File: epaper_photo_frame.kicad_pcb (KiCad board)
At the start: 2 copper layers, 98 parts, among them IC1 ST1PS03AQTR, IC2 CM1624-08DE, J1 47352-1001, J2 Conn_ARM_JTAG_SWD_20, J3 Battery Connector, J4 54104-5031, Q1 BSS138, Q2 SI2301CDS-T1-E3, Q3 AO3401A, Q31 AO3401A, Q32 S8050, U1 SIP32402ADNP-T1GE4, U2 RT9193-33GB, U3 STM32L431CBT6, Y1 NX3215SA-32.768K-STD-MUA-14

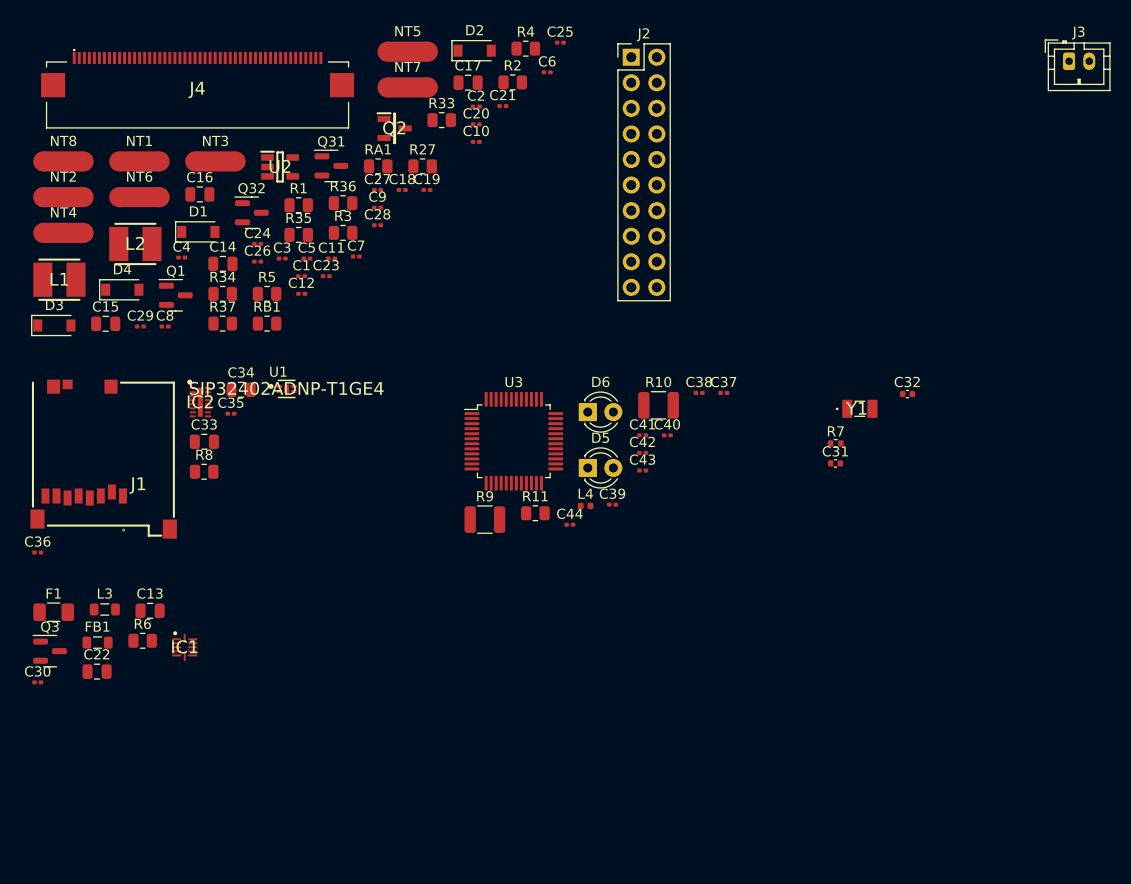
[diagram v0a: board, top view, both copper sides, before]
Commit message: Added preliminary PCL layout
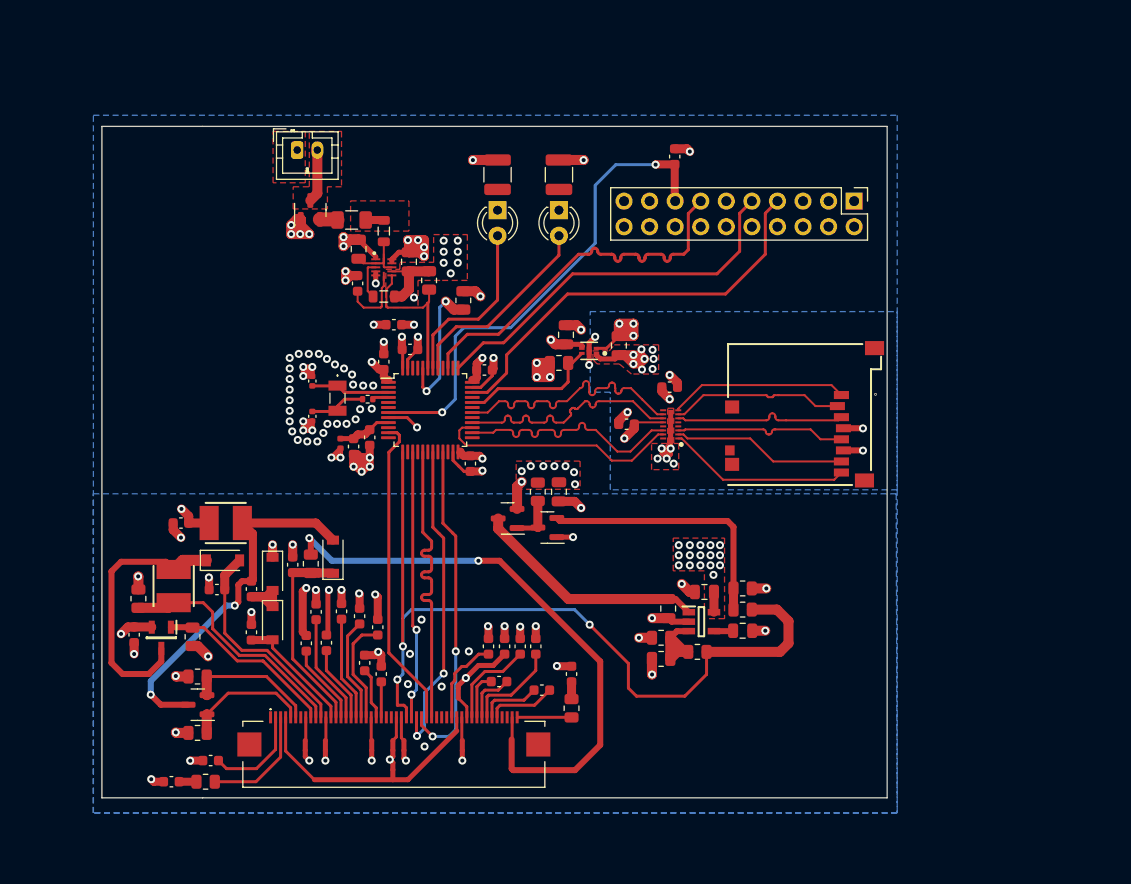
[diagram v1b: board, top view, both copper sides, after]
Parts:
- C1, C10, C11, C12, C18, C19, C2, C20, C21, C23, C24, C25, C26, C27, C28, C29, C3, C30, C35, C36, C37, C38, C39, C4, C40, C41, C42, C43, C44, C5, C6, C7, C8, C9: footprint Capacitor_SMD:C_0201_0603Metric -> Capacitor_SMD:C_0603_1608Metric
- NT1, NT2, NT3, NT4, NT5, NT6, NT7, NT8: footprint NetTie:NetTie-2_SMD_Pad2.0mm -> NetTie:NetTie-2_SMD_Pad0.5mm
- moved J3 77.2 mm to (126.4, 77.2)
- moved C2 73.6 mm to (113.9, 139.9), turned to 180 degrees
- moved J1 72.8 mm to (184.4, 96.4), turned to 90 degrees
- moved J4 68.3 mm to (136.0, 133.9)
- moved R4 67.1 mm to (116.0, 125.5), turned to 90 degrees
- moved R2 66.8 mm to (116.5, 129.4), turned to 180 degrees
- moved NT7 65.9 mm to (129.2, 136.3), turned to -90 degrees
- moved NT2 64.1 mm to (137.0, 136.3), turned to -90 degrees
- moved NT5 63.9 mm to (142.4, 131.1), turned to 90 degrees
- moved C16 63.8 mm to (166.8, 121.0)
- moved C25 63.8 mm to (146.4, 129.9), turned to 180 degrees
- moved RA1 63.5 mm to (117.3, 139.9), turned to 180 degrees
- moved NT3 63.0 mm to (142.8, 136.3), turned to -90 degrees
- moved NT8 62.8 mm to (127.2, 136.3), turned to -90 degrees
- moved NT6 62.7 mm to (135.9, 139.2), turned to 90 degrees
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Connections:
- IC2 pad 1: unconnected-(IC2-Pad1) -> /Micro SD/SD_DATA1
- IC2 pad 10: /Micro SD/SD_DATA3 -> /MCU/SDC_SPI_NSS
- IC2 pad 11: /Micro SD/SD_CMD -> /MCU/SDC_SPI_MOSI
- IC2 pad 14: /Micro SD/SD_CLK -> /MCU/SDC_SPI_SCK
- IC2 pad 15: /Micro SD/SD_DATA0 -> /MCU/SDC_SPI_MISO
- IC2 pad 16: /Micro SD/SD_DATA1 -> unconnected-(IC2-Pad16)
- IC2 pad 2: /MCU/SDC_SPI_MISO -> /Micro SD/SD_DATA0
- IC2 pad 3: /MCU/SDC_SPI_SCK -> /Micro SD/SD_CLK
- IC2 pad 6: /MCU/SDC_SPI_MOSI -> /Micro SD/SD_CMD
- IC2 pad 7: /MCU/SDC_SPI_NSS -> /Micro SD/SD_DATA3
- IC2 pad 8: unconnected-(IC2-Pad8) -> /Micro SD/SD_DATA2
- IC2 pad 9: /Micro SD/SD_DATA2 -> unconnected-(IC2-Pad9)
- J4 pad 34: /Display Adapter/EPD_D1 -> unconnected-(J4-Pad34)
- J4 pad 35: /Display Adapter/EPD_D2 -> unconnected-(J4-Pad35)
- J4 pad 36: /Display Adapter/EPD_D3 -> unconnected-(J4-Pad36)
- U3 pad 13: /Display Adapter/EPD_CS -> /Display Adapter/EPD_RST
- U3 pad 15: /Display Adapter/EPD_DC -> /Display Adapter/EPD_BUSY
- U3 pad 19: /Display Adapter/EPD_RST -> /Display Adapter/EPD_DC
- U3 pad 21: /Display Adapter/EPD_BUSY -> /Display Adapter/EPD_CS
- U3 pad 41: unconnected-(U3-Pad41) -> /MCU/LED_ERR_IN
- U3 pad 42: unconnected-(U3-Pad42) -> /MCU/LED_BUSY_IN
- U3 pad 45: /MCU/LED_ERR_IN -> unconnected-(U3-Pad45)
- U3 pad 46: /MCU/LED_BUSY_IN -> unconnected-(U3-Pad46)
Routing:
- net GND: track 0.00 -> 181.5 mm, vias 0 -> 120
- net /Display Adapter/EPD_RST: track 0.00 -> 83.6 mm, vias 0 -> 3
- net /Display Adapter/VGH: track 0.00 -> 59.0 mm, vias 0 -> 2
- net /Debug Connector/NRST: track 0.00 -> 49.3 mm, vias 0 -> 2
- net /Debug Connector/SWDIO: track 0.00 -> 41.6 mm
- net /Debug Connector/SWDCLK: track 0.00 -> 38.3 mm
- net /Debug Connector/SWO: track 0.00 -> 38.1 mm
- net /Display Adapter/3v3_HPF: track 0.00 -> 36.6 mm, vias 0 -> 2
- net /Display Adapter/EPD_CS: track 0.00 -> 33.0 mm, vias 0 -> 2
- net /Display Adapter/EPD_DC: track 0.00 -> 31.7 mm, vias 0 -> 2
- net /Display Adapter/EPD_SCK: track 0.00 -> 31.2 mm
- net /Display Adapter/EPD_DIN: track 0.00 -> 31.0 mm
- net /Debug Connector/MCU_VDD: track 0.00 -> 29.2 mm, vias 0 -> 24
- net /MCU/SDC_SPI_NSS: track 0.00 -> 26.9 mm
- net /Display Adapter/VPC_1: track 0.00 -> 26.8 mm
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- added copper zone on B.Cu, net /Debug Connector/MCU_VDD
- added copper zone on F.Cu, net /Debug Connector/MCU_VDD
- added copper zone on B.Cu, net /Display Adapter/3v3
- added copper zone on F.Cu, net /Display Adapter/3v3
- added copper zone on B.Cu, net /Micro SD/3v3
- added copper zone on F.Cu, net /Micro SD/3v3
- added copper zone on F.Cu, net /Power Supply/VBAT_IN
- added copper zone on F.Cu, net /Power Supply/VBAT_IN_FUSE_CHECKED
- added copper zone on F.Cu, net GND
- added copper zone on In1.Cu, net GND
- added copper zone on In2.Cu, net GND
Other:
- board outline added: 78 x 66.7 mm
- copper layers 2 -> 4
- rule pad_to_mask_clearance: 0 -> 0.06

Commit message: Revision 1 of the board that was manufactured
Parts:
- added H1: MountingHole, MountingHole:MountingHole_3.2mm_M3, F.Cu at (105.8, 75.7)
- added H2: MountingHole, MountingHole:MountingHole_3.2mm_M3, F.Cu at (181.2, 75.7)
- added H3: MountingHole, MountingHole:MountingHole_3.2mm_M3, F.Cu at (105.8, 137.7)
- added H4: MountingHole, MountingHole:MountingHole_3.2mm_M3, F.Cu at (181.2, 137.7)
- added R12: 5k, Resistor_SMD:R_1206_3216Metric, F.Cu at (142.0, 78.2)
- Q32: footprint Package_TO_SOT_SMD:SOT-23 -> Package_TO_SOT_SMD:SOT-23-3
- R10: value 42R2 -> 47k
- R9: value 78R7 -> 47k
- moved C38 0.50 mm to (136.0, 94.0)
- moved Q32 0.11 mm to (151.4, 114.7)
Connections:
- R10 pad 2: GND -> /MCU/LED_BUSY_OUT_2
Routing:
- net /Display Adapter/GNDA+(GND): track 4.64 -> 9.61 mm
- net /Debug Connector/SWDCLK: track 38.3 -> 41.4 mm
- net /Debug Connector/SWO: track 38.1 -> 35.1 mm
- net /MCU/LED_BUSY_OUT_2: track 0.00 -> 2.91 mm
- net /MCU/SDC_SPI_NSS: track 26.9 -> 24.3 mm
- net /MCU/LED_ERR_OUT: track 0.00 -> 2.06 mm
- net /MCU/LED_BUSY_OUT: track 0.00 -> 2.06 mm
- net (no net): track 0.75 -> 0.00 mm
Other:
- board size 78 x 66.7 mm -> 83.1 x 69.5 mm
- rule pad_to_mask_clearance: 0.06 -> 0.05
- board text added: "+"
- board text added: "JLCJLCJLCJLC"

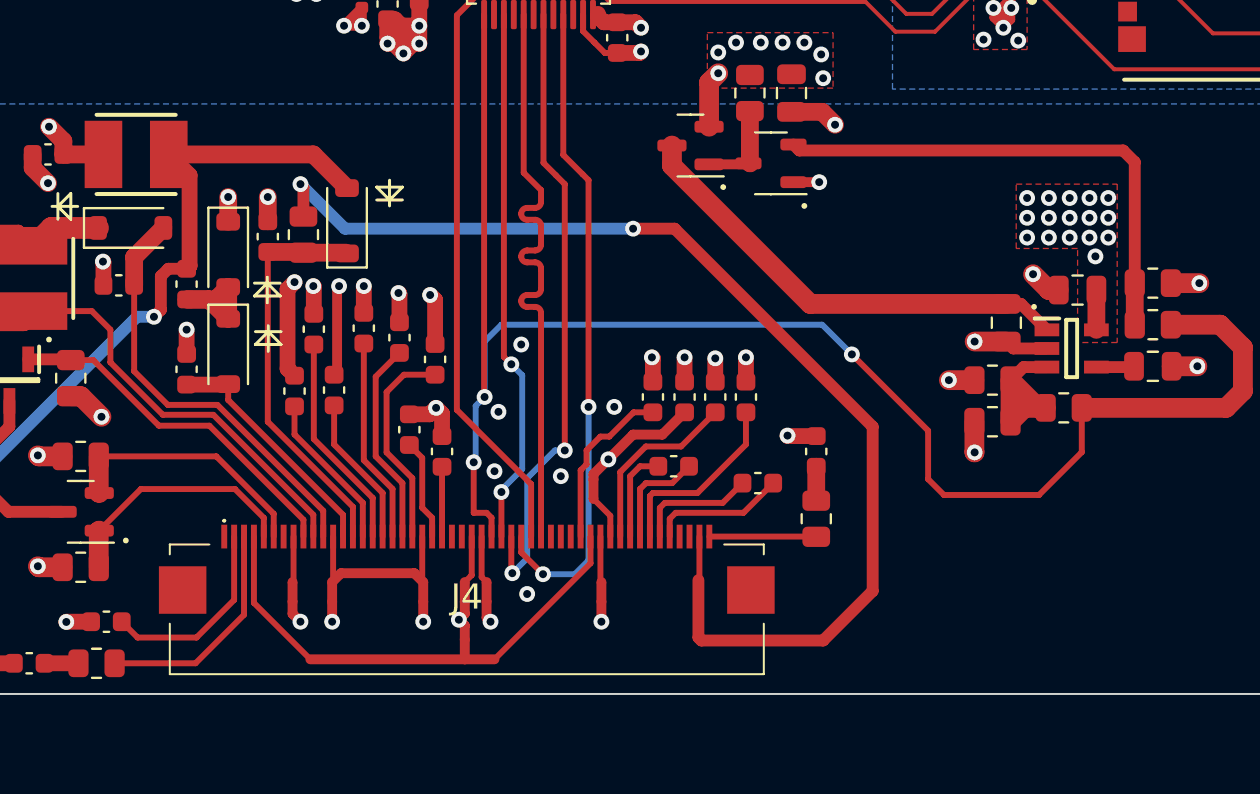
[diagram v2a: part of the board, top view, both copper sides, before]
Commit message: Fix NPN BJT Base and emitter pin swap. Attach BS0 to GND to select 4 pin SPI mode for Epaper display. Use 2 side FPC connector
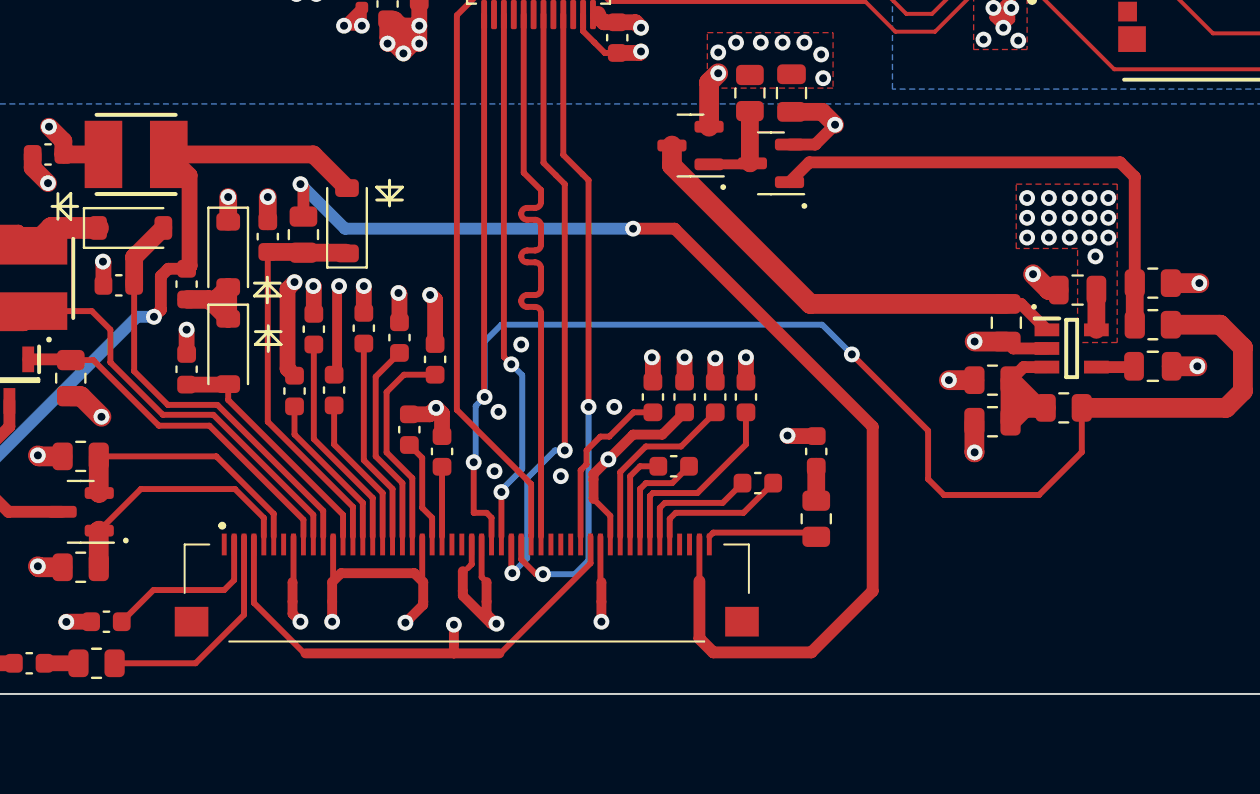
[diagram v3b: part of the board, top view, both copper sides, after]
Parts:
- J4: value 54104-5031 -> XF2M50151A; footprint SamacSys_Parts:541045031 -> SamacSys_Parts:XF2M50151A
- Q32: value S8050 -> MMSS8050; footprint Package_TO_SOT_SMD:SOT-23-3 -> Package_TO_SOT_SMD:SOT-23
- moved J4 2.45 mm to (136.0, 136.3)
- moved NT6 0.93 mm to (135.3, 138.4)
- moved NT4 0.56 mm to (135.8, 135.8)
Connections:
- NT4 pad 2: /Display Adapter/3v3 -> GND
- Q32 pad 1: GND -> /Display Adapter/EPD_RST_INT
- Q32 pad 2: /Display Adapter/EPD_RST_INT -> GND
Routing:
- net GND: track 181.6 -> 185.9 mm, vias 120 -> 118
- net /Display Adapter/3v3: track 19.4 -> 17.2 mm
- net /Display Adapter/TFT VCOM: track 9.99 -> 8.74 mm
- net /Display Adapter/BS0: track 2.44 -> 1.68 mm
